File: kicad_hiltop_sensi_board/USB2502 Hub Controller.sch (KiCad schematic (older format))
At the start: 39 parts, among them U27 USB2502, U7 AT24C02C-SSHM-T, Y1 50ppm 24.000MHZ

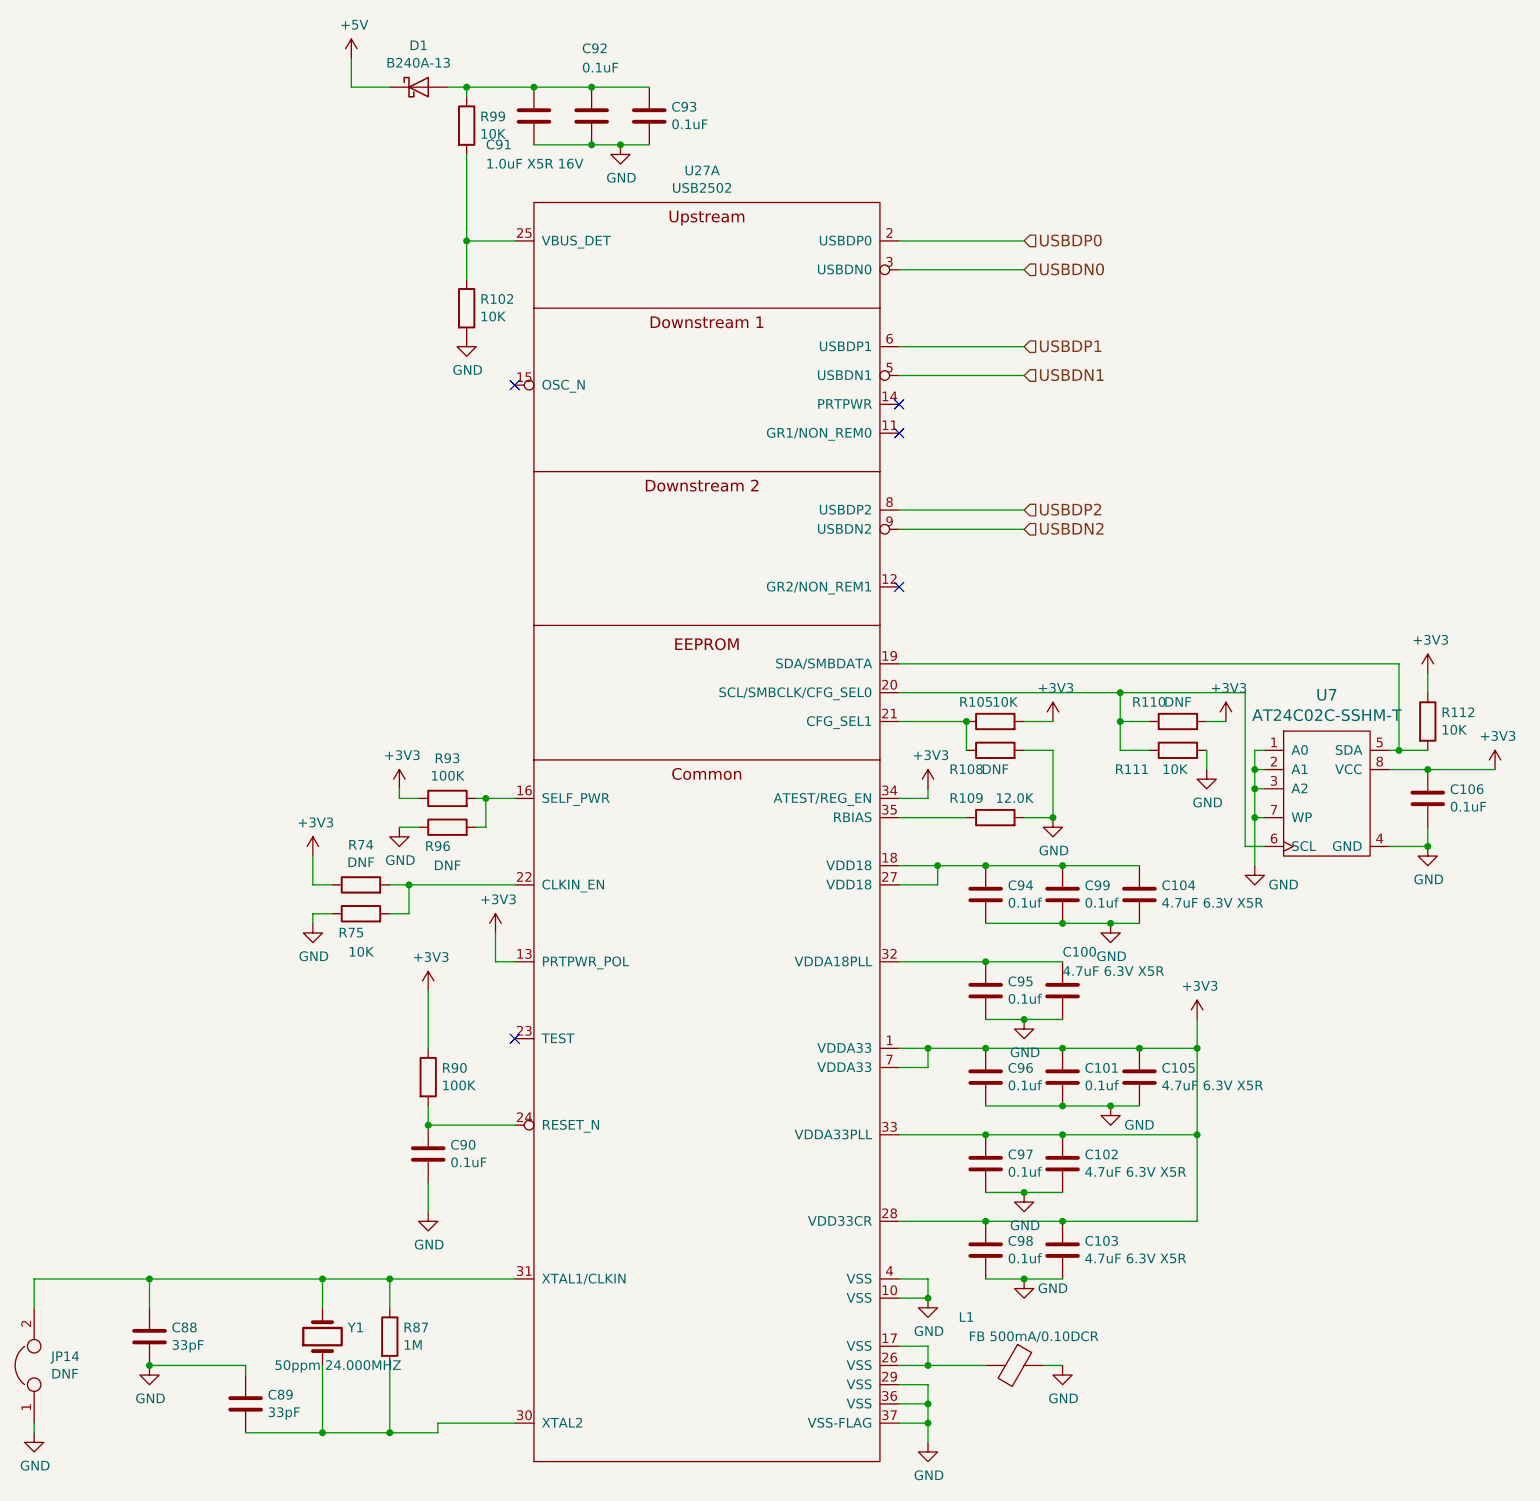
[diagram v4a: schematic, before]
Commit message: Updated sensi board pin map and layout before PCB tracking
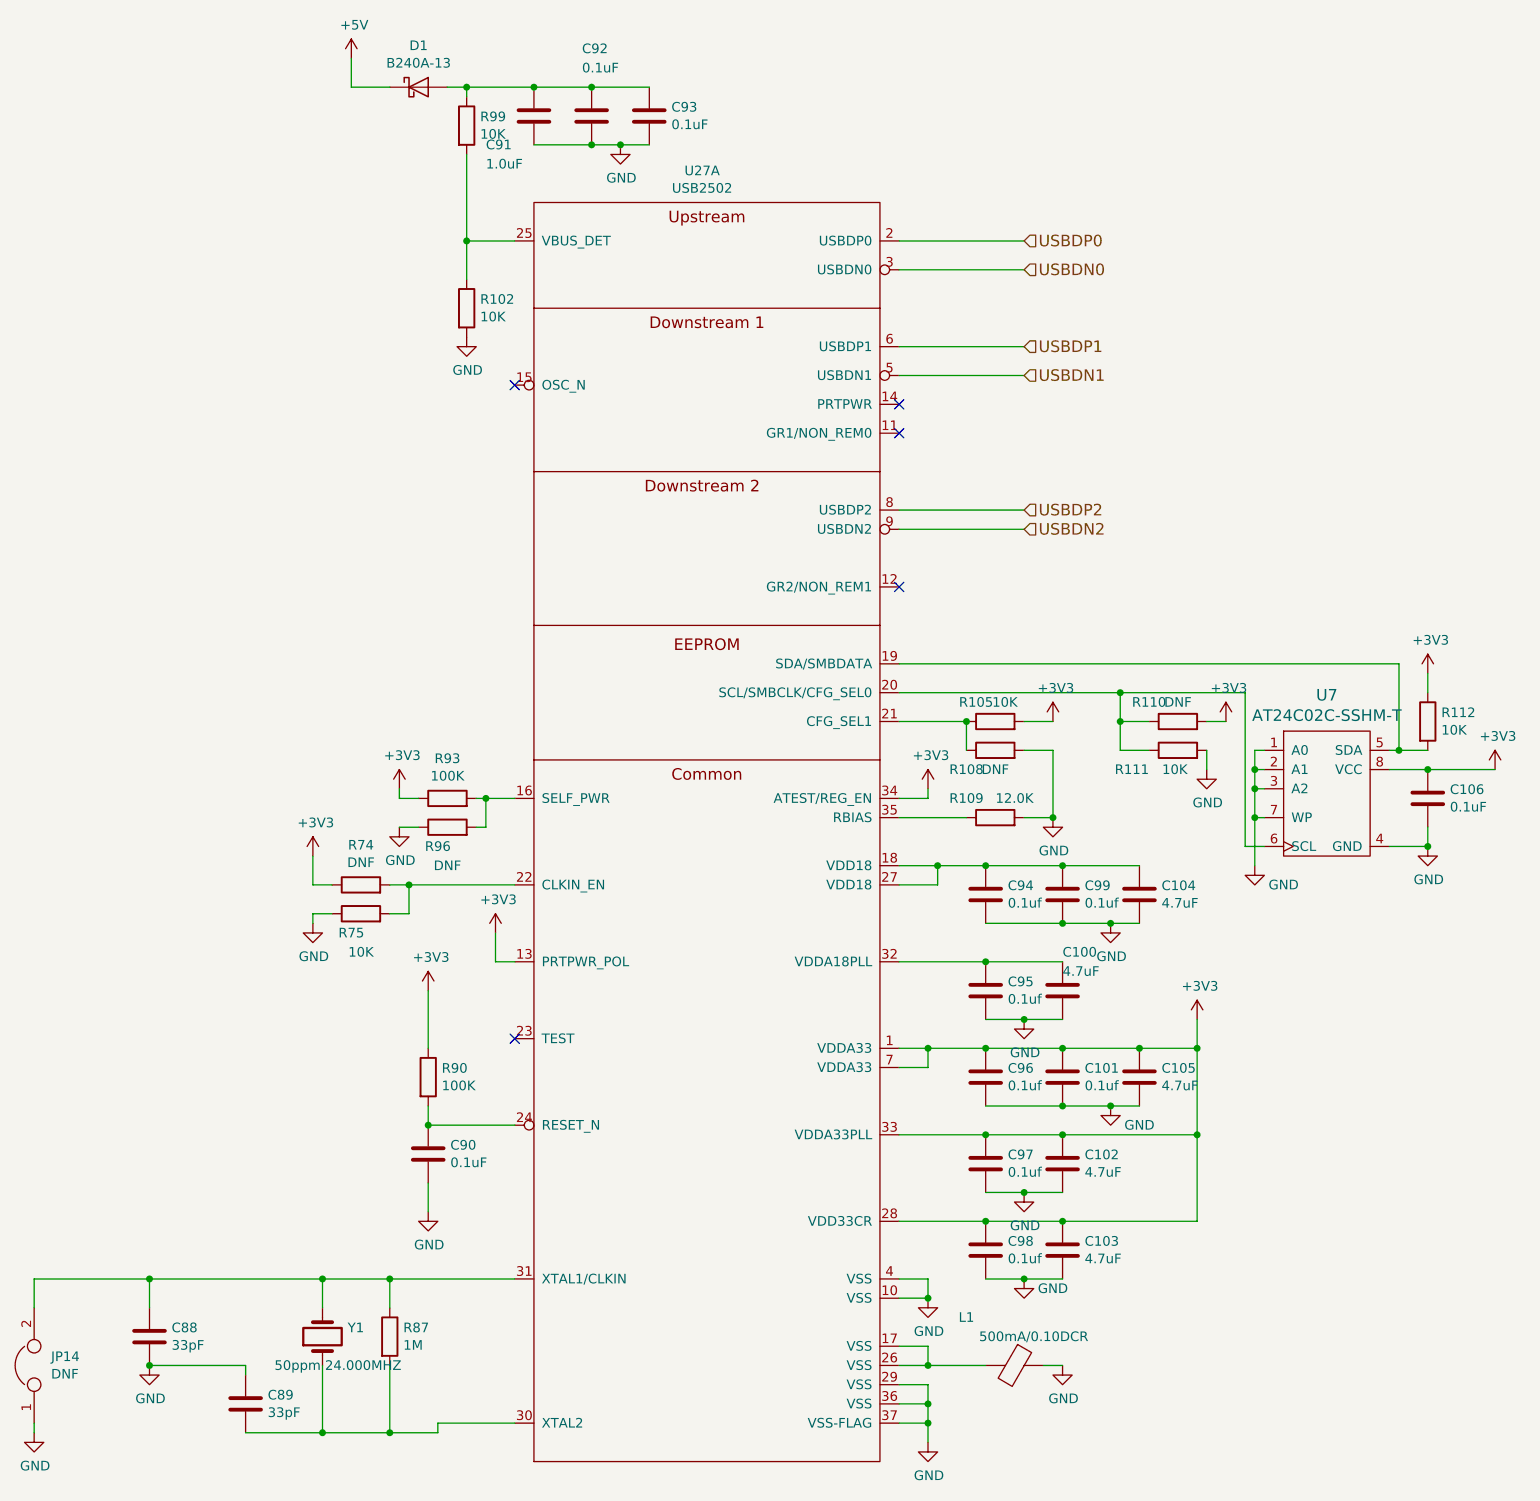
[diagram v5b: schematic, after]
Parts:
- C100, C102, C103, C104, C105: value 4.7uF 6.3V X5R -> 4.7uF; Devtank (none) -> 105-025; Dielectric (none) -> X5R; Voltage (none) -> 6.3V
- C101, C106, C92, C93, C94, C95, C96, C97, C98, C99: Devtank (none) -> 105-019
- C88, C89: Devtank (none) -> 106-015
- C90: Devtank (none) -> 105-002
- C91: value 1.0uF X5R 16V -> 1.0uF; Devtank (none) -> 105-026; Dielectric (none) -> X5R; Voltage (none) -> 16V
- D1: Devtank (none) -> 133-008
- JP14: footprint Connector_PinHeader_1.00mm:PinHeader_1x02_P1.00mm_Vertical -> Connector_PinHeader_2.54mm:PinHeader_1x02_P2.54mm_Vertical; Devtank (none) -> 710-002
- L1: value FB 500mA/0.10DCR -> 500mA/0.10DCR
- R102, R105, R111, R112, R75, R99: Devtank (none) -> 101-010
- R109: footprint Resistor_SMD:R_0402_1005Metric -> Resistor_SMD:R_0603_1608Metric; Devtank (none) -> 101-050
- R87: footprint Resistor_SMD:R_0402_1005Metric -> Resistor_SMD:R_0603_1608Metric; Devtank (none) -> 101-056
- R90, R93: Devtank (none) -> 101-015
- U27: Devtank (none) -> 118-012
- U7: Devtank (none) -> 129-006
- Y1: Devtank (none) -> 181-010
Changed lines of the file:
@@
 F 2 "Package_DFN_QFN:QFN-36-1EP_6x6mm_P0.5mm_EP4.1x4.1mm" H 6900 -350 50  0001 C CNN
 F 3 "DOCUMENTATION" H 7050 -250 50  0001 C CNN
+F 4 "118-012" H 6150 4500 50  0001 C CNN "Devtank"
 	1    6150 4500
 	1    0    0    -1
@@
 F 2 "Crystal:Crystal_SMD_TXC_7A-2Pin_5x3.2mm" H 4150 8550 50  0001 C CNN
 F 3 "" H 4150 8550 50  0001 C CNN
+F 4 "181-010" H 4150 8550 50  0001 C CNN "Devtank"
 	1    4150 8550
 	0    -1   -1   0
@@
 F 2 "Capacitor_SMD:C_0402_1005Metric" H 8038 7050 50  0001 C CNN
 F 3 "" H 8000 7200 50  0001 C CNN
+F 4 "105-019" H 8000 7200 50  0001 C CNN "Devtank"
 	1    8000 7200
 	1    0    0    -1
@@
 P 8400 7200
 F 0 "C105" H 8515 7246 50  0000 L CNN
-F 1 "4.7uF 6.3V X5R" H 8515 7155 50  0000 L CNN
+F 1 "4.7uF " H 8515 7155 50  0000 L CNN
 F 2 "Capacitor_SMD:C_0402_1005Metric" H 8438 7050 50  0001 C CNN
 F 3 "" H 8400 7200 50  0001 C CNN
+F 4 "6.3V" H 8400 7200 50  0001 C CNN "Voltage"
+F 5 "X5R" H 8400 7200 50  0001 C CNN "Dielectric"
+F 6 "105-025" H 8400 7200 50  0001 C CNN "Devtank"
 	1    8400 7200
 	1    0    0    -1
@@
 F 2 "Capacitor_SMD:C_0402_1005Metric" H 7638 7050 50  0001 C CNN
 F 3 "" H 7600 7200 50  0001 C CNN
+F 4 "105-019" H 7600 7200 50  0001 C CNN "Devtank"
 	1    7600 7200
 	1    0    0    -1
@@
 F 2 "Capacitor_SMD:C_0402_1005Metric" H 7638 7500 50  0001 C CNN
 F 3 "" H 7600 7650 50  0001 C CNN
+F 4 "105-019" H 7600 7650 50  0001 C CNN "Devtank"
 	1    7600 7650
 	1    0    0    -1
@@
 P 8000 7650
 F 0 "C102" H 8115 7696 50  0000 L CNN
-F 1 "4.7uF 6.3V X5R" H 8115 7605 50  0000 L CNN
+F 1 "4.7uF" H 8115 7605 50  0000 L CNN
 F 2 "Capacitor_SMD:C_0402_1005Metric" H 8038 7500 50  0001 C CNN
 F 3 "" H 8000 7650 50  0001 C CNN
+F 4 "6.3V" H 8000 7650 50  0001 C CNN "Voltage"
+F 5 "X5R" H 8000 7650 50  0001 C CNN "Dielectric"
+F 6 "105-025" H 8000 7650 50  0001 C CNN "Devtank"
 	1    8000 7650
 	1    0    0    -1
@@
 F 2 "Capacitor_SMD:C_0402_1005Metric" H 7638 6600 50  0001 C CNN
 F 3 "" H 7600 6750 50  0001 C CNN
+F 4 "105-019" H 7600 6750 50  0001 C CNN "Devtank"
 	1    7600 6750
 	1    0    0    -1
@@
 P 8000 6750
 F 0 "C100" H 8000 6950 50  0000 L CNN
-F 1 "4.7uF 6.3V X5R" H 8000 6850 50  0000 L CNN
+F 1 "4.7uF " H 8000 6850 50  0000 L CNN
 F 2 "Capacitor_SMD:C_0402_1005Metric" H 8038 6600 50  0001 C CNN
 F 3 "" H 8000 6750 50  0001 C CNN
+F 4 "6.3V" H 8000 6750 50  0001 C CNN "Voltage"
+F 5 "X5R" H 8000 6750 50  0001 C CNN "Dielectric"
+F 6 "105-025" H 8000 6750 50  0001 C CNN "Devtank"
 	1    8000 6750
 	1    0    0    -1
@@
 F 2 "Capacitor_SMD:C_0402_1005Metric" H 8038 6100 50  0001 C CNN
 F 3 "" H 8000 6250 50  0001 C CNN
+F 4 "105-019" H 8000 6250 50  0001 C CNN "Devtank"
 	1    8000 6250
 	1    0    0    -1
@@
 P 8400 6250
 F 0 "C104" H 8515 6296 50  0000 L CNN
-F 1 "4.7uF 6.3V X5R" H 8515 6205 50  0000 L CNN
+F 1 "4.7uF" H 8515 6205 50  0000 L CNN
 F 2 "Capacitor_SMD:C_0402_1005Metric" H 8438 6100 50  0001 C CNN
 F 3 "" H 8400 6250 50  0001 C CNN
+F 4 "6.3V" H 8400 6250 50  0001 C CNN "Voltage"
+F 5 "X5R" H 8400 6250 50  0001 C CNN "Dielectric"
+F 6 "105-025" H 8400 6250 50  0001 C CNN "Devtank"
 	1    8400 6250
 	1    0    0    -1
@@
 F 2 "Capacitor_SMD:C_0402_1005Metric" H 7638 6100 50  0001 C CNN
 F 3 "" H 7600 6250 50  0001 C CNN
+F 4 "105-019" H 7600 6250 50  0001 C CNN "Devtank"
 	1    7600 6250
 	1    0    0    -1
@@
 F 2 "Capacitor_SMD:C_0402_1005Metric" H 9938 5600 50  0001 C CNN
 F 3 "" H 9900 5750 50  0001 C CNN
+F 4 "105-019" H 9900 5750 50  0001 C CNN "Devtank"
 	1    9900 5750
 	1    0    0    -1
@@
 F 2 "Resistor_SMD:R_0603_1608Metric" V 7580 5350 50  0001 C CNN
 F 3 "" H 7650 5350 50  0001 C CNN
+F 4 "101-010" H 7650 5350 50  0001 C CNN "Devtank"
 	1    7650 5350
 	0    -1   -1   0
@@
 F 2 "Resistor_SMD:R_0603_1608Metric" V 8530 5500 50  0001 C CNN
 F 3 "" H 8600 5500 50  0001 C CNN
+F 4 "101-010" H 8600 5500 50  0001 C CNN "Devtank"
 	1    8600 5500
 	0    -1   -1   0
@@
 F 2 "Resistor_SMD:R_0603_1608Metric" V 9830 5350 50  0001 C CNN
 F 3 "" H 9900 5350 50  0001 C CNN
+F 4 "101-010" H 9900 5350 50  0001 C CNN "Devtank"
 	1    9900 5350
 	1    0    0    -1
@@
 F 2 "Resistor_SMD:R_0603_1608Metric" V 4280 6350 50  0001 C CNN
 F 3 "" H 4350 6350 50  0001 C CNN
+F 4 "101-010" H 4350 6350 50  0001 C CNN "Devtank"
 	1    4350 6350
 	0    -1   -1   0
@@
 F 2 "Resistor_SMD:R_0603_1608Metric" V 4630 7200 50  0001 C CNN
 F 3 "" H 4700 7200 50  0001 C CNN
+F 4 "101-015" H 4700 7200 50  0001 C CNN "Devtank"
 	1    4700 7200
 	1    0    0    -1
@@
 F 0 "R87" H 4570 8596 50  0000 L CNN
 F 1 "1M" H 4570 8505 50  0000 L CNN
-F 2 "Resistor_SMD:R_0402_1005Metric" V 4430 8550 50  0001 C CNN
+F 2 "Resistor_SMD:R_0603_1608Metric" V 4430 8550 50  0001 C CNN
 F 3 "" H 4500 8550 50  0001 C CNN
+F 4 "101-056" H 4500 8550 50  0001 C CNN "Devtank"
 	1    4500 8550
 	1    0    0    -1
@@
 F 2 "Resistor_SMD:R_0603_1608Metric" V 4730 5750 50  0001 C CNN
 F 3 "" H 4800 5750 50  0001 C CNN
+F 4 "101-015" H 4800 5750 50  0001 C CNN "Devtank"
 	1    4800 5750
 	0    -1   -1   0
@@
 F 2 "Capacitor_SMD:C_0603_1608Metric" H 3288 8400 50  0001 C CNN
 F 3 "" H 3250 8550 50  0001 C CNN
+F 4 "106-015" H 3250 8550 50  0001 C CNN "Devtank"
 	1    3250 8550
 	1    0    0    -1
@@
 F 2 "Capacitor_SMD:C_0603_1608Metric" H 3788 8750 50  0001 C CNN
 F 3 "" H 3750 8900 50  0001 C CNN
+F 4 "106-015" H 3750 8900 50  0001 C CNN "Devtank"
 	1    3750 8900
 	1    0    0    -1
@@
 F 2 "Capacitor_SMD:C_0603_1608Metric" H 4738 7450 50  0001 C CNN
 F 3 "" H 4700 7600 50  0001 C CNN
+F 4 "105-002" H 4700 7600 50  0001 C CNN "Devtank"
 	1    4700 7600
 	1    0    0    -1
@@
 F 0 "JP14" V 2696 8612 50  0000 R CNN
 F 1 "DNF" V 2605 8612 50  0000 R CNN
-F 2 "Connector_PinHeader_1.00mm:PinHeader_1x02_P1.00mm_Vertical" H 2650 8700 50  0001 C CNN
+F 2 "Connector_PinHeader_2.54mm:PinHeader_1x02_P2.54mm_Vertical" H 2650 8700 50  0001 C CNN
 F 3 "" H 2650 8700 50  0001 C CNN
+F 4 "710-002" H 2650 8700 50  0001 C CNN "Devtank"
 	1    2650 8700
 	0    -1   -1   0
@@
 F 0 "R109" V 7750 6000 50  0000 C CNN
 F 1 "12.0K " V 7750 5750 50  0000 C CNN
-F 2 "Resistor_SMD:R_0402_1005Metric" V 7580 5850 50  0001 C CNN
+F 2 "Resistor_SMD:R_0603_1608Metric" V 7580 5850 50  0001 C CNN
 F 3 "" H 7650 5850 50  0001 C CNN
 F 4 "1%" V 7650 5850 50  0001 C CNN "Tolerance"
+F 5 "101-050" H 7650 5850 50  0001 C CNN "Devtank"
 	1    7650 5850
 	0    -1   -1   0
@@
 P 8000 8100
 F 0 "C103" H 8115 8146 50  0000 L CNN
-F 1 "4.7uF 6.3V X5R" H 8115 8055 50  0000 L CNN
+F 1 "4.7uF " H 8115 8055 50  0000 L CNN
 F 2 "Capacitor_SMD:C_0402_1005Metric" H 8038 7950 50  0001 C CNN
 F 3 "" H 8000 8100 50  0001 C CNN
+F 4 "6.3V" H 8000 8100 50  0001 C CNN "Voltage"
+F 5 "X5R" H 8000 8100 50  0001 C CNN "Dielectric"
+F 6 "105-025" H 8000 8100 50  0001 C CNN "Devtank"
 	1    8000 8100
 	1    0    0    -1
@@
 F 2 "Capacitor_SMD:C_0402_1005Metric" H 7638 7950 50  0001 C CNN
 F 3 "" H 7600 8100 50  0001 C CNN
+F 4 "105-019" H 7600 8100 50  0001 C CNN "Devtank"
 	1    7600 8100
 	1    0    0    -1
@@
 P 7750 8700
 F 0 "L1" V 7500 8450 50  0000 C CNN
-F 1 "FB 500mA/0.10DCR" V 7600 8800 50  0000 C CNN
+F 1 "500mA/0.10DCR" V 7600 8800 50  0000 C CNN
 F 2 "Inductor_SMD:L_0805_2012Metric" V 7680 8700 50  0001 C CNN
 F 3 "" H 7750 8700 50  0001 C CNN
@@
 F 2 "Diode_SMD:D_SMA" H 4650 2050 50  0001 C CNN
 F 3 "" H 4650 2050 50  0001 C CNN
+F 4 "133-008" H 4650 2050 50  0001 C CNN "Devtank"
 	1    4650 2050
 	1    0    0    -1
@@
 P 5250 2200
 F 0 "C91" H 5000 2050 50  0000 L CNN
-F 1 "1.0uF X5R 16V" H 5000 1950 50  0000 L CNN
+F 1 "1.0uF " H 5000 1950 50  0000 L CNN
 F 2 "Capacitor_SMD:C_0402_1005Metric" H 5288 2050 50  0001 C CNN
 F 3 "" H 5250 2200 50  0001 C CNN
+F 4 "16V" H 5250 2200 50  0001 C CNN "Voltage"
+F 5 "X5R" H 5250 2200 50  0001 C CNN "Dielectric"
+F 6 "105-026" H 5250 2200 50  0001 C CNN "Devtank"
 	1    5250 2200
 	1    0    0    -1
@@
 F 2 "Capacitor_SMD:C_0402_1005Metric" H 5588 2050 50  0001 C CNN
 F 3 "" H 5550 2200 50  0001 C CNN
+F 4 "105-019" H 5550 2200 50  0001 C CNN "Devtank"
 	1    5550 2200
 	1    0    0    -1
@@
 F 2 "Capacitor_SMD:C_0402_1005Metric" H 5888 2050 50  0001 C CNN
 F 3 "" H 5850 2200 50  0001 C CNN
+F 4 "105-019" H 5850 2200 50  0001 C CNN "Devtank"
 	1    5850 2200
 	1    0    0    -1
@@
 F 2 "Resistor_SMD:R_0603_1608Metric" V 4830 2250 50  0001 C CNN
 F 3 "" H 4900 2250 50  0001 C CNN
+F 4 "101-010" H 4900 2250 50  0001 C CNN "Devtank"
 	1    4900 2250
 	1    0    0    -1
@@
 F 2 "Resistor_SMD:R_0603_1608Metric" V 4830 3200 50  0001 C CNN
 F 3 "" H 4900 3200 50  0001 C CNN
+F 4 "101-010" H 4900 3200 50  0001 C CNN "Devtank"
 	1    4900 3200
 	1    0    0    -1
@@
 F 2 "Package_SO:SOIC-8_3.9x4.9mm_P1.27mm" H 9300 5150 60  0001 C CNN
 F 3 "" H 9300 5150 60  0001 C CNN
+F 4 "129-006" H 9350 5700 50  0001 C CNN "Devtank"
 	1    9350 5700
 	1    0    0    -1

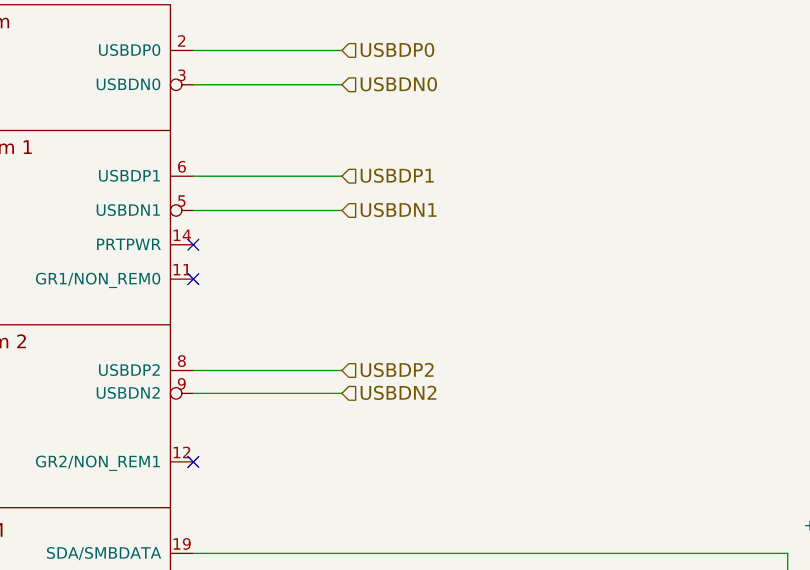
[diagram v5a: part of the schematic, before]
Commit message: Started PCB routing of Sensi Board LBBC
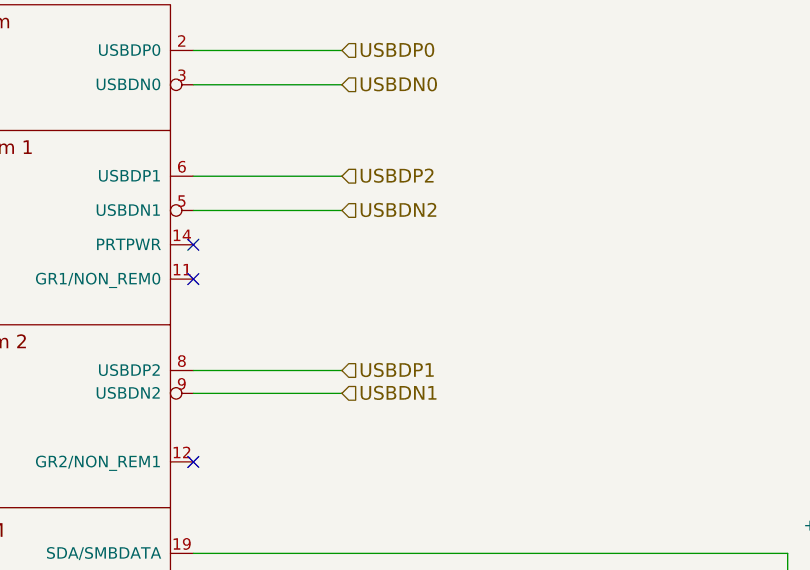
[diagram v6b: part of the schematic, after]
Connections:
- net USBDN1: now also U27.9 (USBDN2); no longer U27.5 (USBDN1)
- net USBDN2: now also U27.5 (USBDN1); no longer U27.9 (USBDN2)
- net USBDP1: now also U27.8 (USBDP2); no longer U27.6 (USBDP1)
- net USBDP2: now also U27.6 (USBDP1); no longer U27.8 (USBDP2)
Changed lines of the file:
@@
 Text HLabel 7800 3000 2    60   Input ~ 0
 USBDN0
+Text HLabel 7800 4250 2    60   Input ~ 0
+USBDP1
+Text HLabel 7800 4350 2    60   Input ~ 0
+USBDN1
 Text HLabel 7800 3400 2    60   Input ~ 0
-USBDP1
+USBDP2
 Text HLabel 7800 3550 2    60   Input ~ 0
-USBDN1
-Text HLabel 7800 4250 2    60   Input ~ 0
-USBDP2
-Text HLabel 7800 4350 2    60   Input ~ 0
 USBDN2
 Wire Wire Line

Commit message: Pre stitching via for sensi board.
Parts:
- U27: footprint Package_DFN_QFN:QFN-36-1EP_6x6mm_P0.5mm_EP4.1x4.1mm -> Package_DFN_QFN:QFN-36-1EP_6x6mm_P0.5mm_EP3.7x3.7mm
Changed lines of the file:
@@
 F 0 "U27" H 6125 6515 50  0000 C CNN
 F 1 "USB2502" H 6125 6424 50  0000 C CNN
-F 2 "Package_DFN_QFN:QFN-36-1EP_6x6mm_P0.5mm_EP4.1x4.1mm" H 6900 -350 50  0001 C CNN
+F 2 "Package_DFN_QFN:QFN-36-1EP_6x6mm_P0.5mm_EP3.7x3.7mm" H 6900 -350 50  0001 C CNN
 F 3 "DOCUMENTATION" H 7050 -250 50  0001 C CNN
 F 4 "118-012" H 6150 4500 50  0001 C CNN "Devtank"
